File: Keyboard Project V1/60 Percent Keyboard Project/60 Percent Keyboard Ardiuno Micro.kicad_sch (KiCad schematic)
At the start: 126 parts, among them J1 Analog, J2 Digital

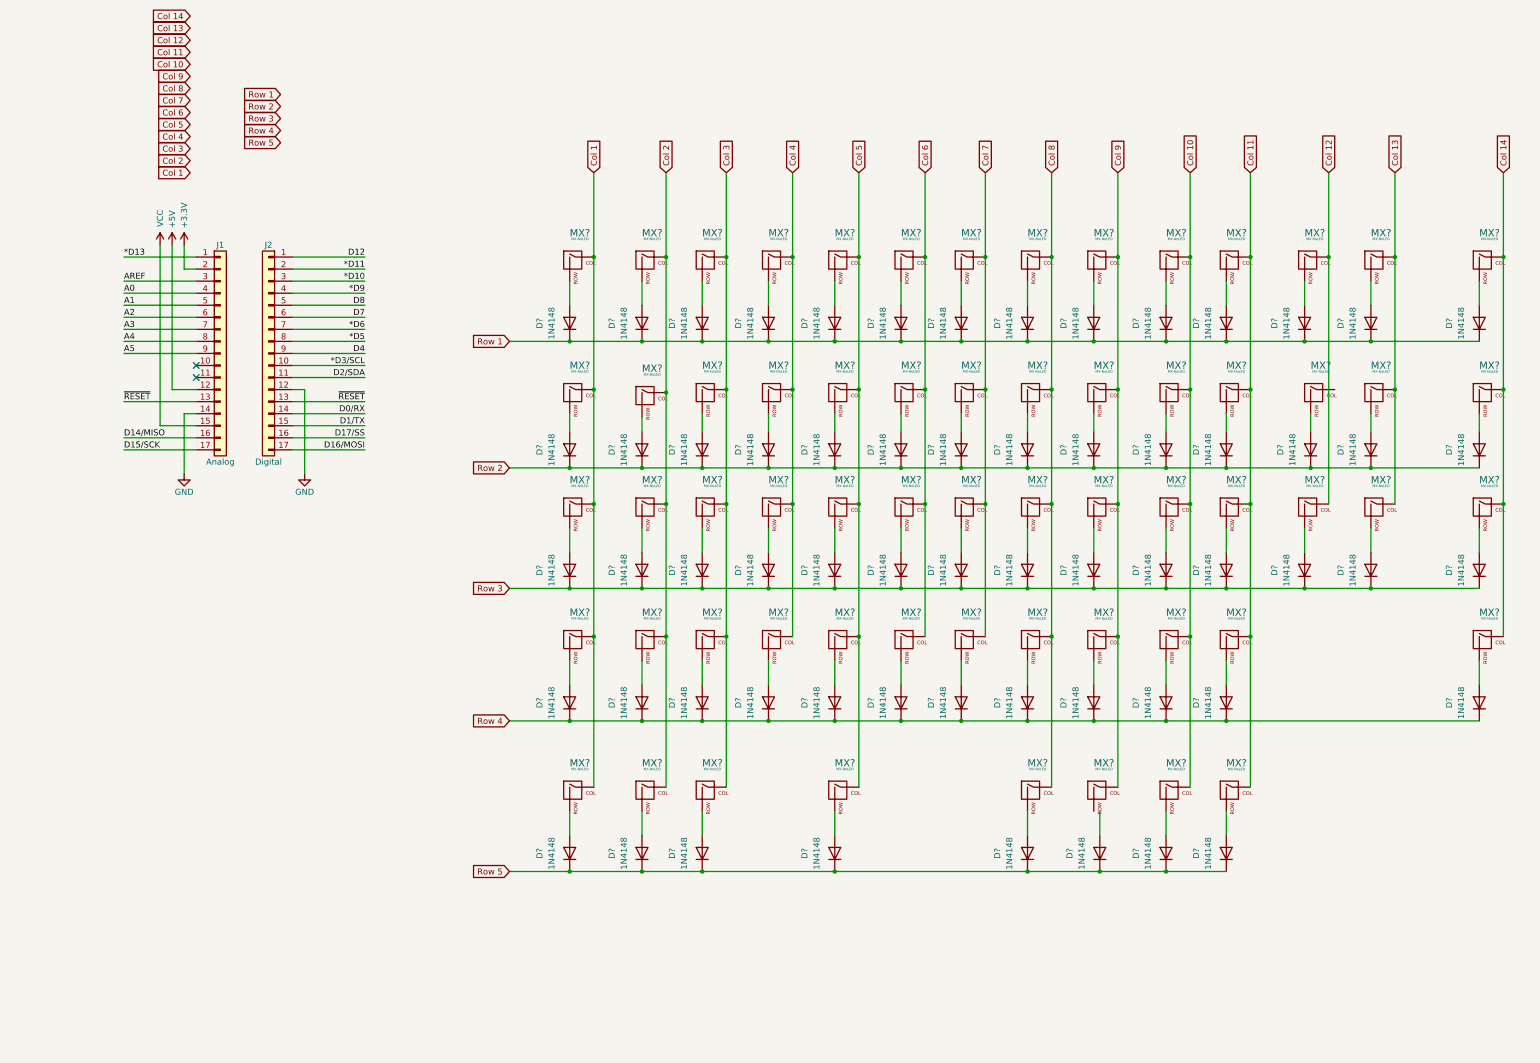
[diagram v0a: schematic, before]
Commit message: updated version of version 1 and currently in the PCB editor. Almost done with version one and may work on version V1.1 after this
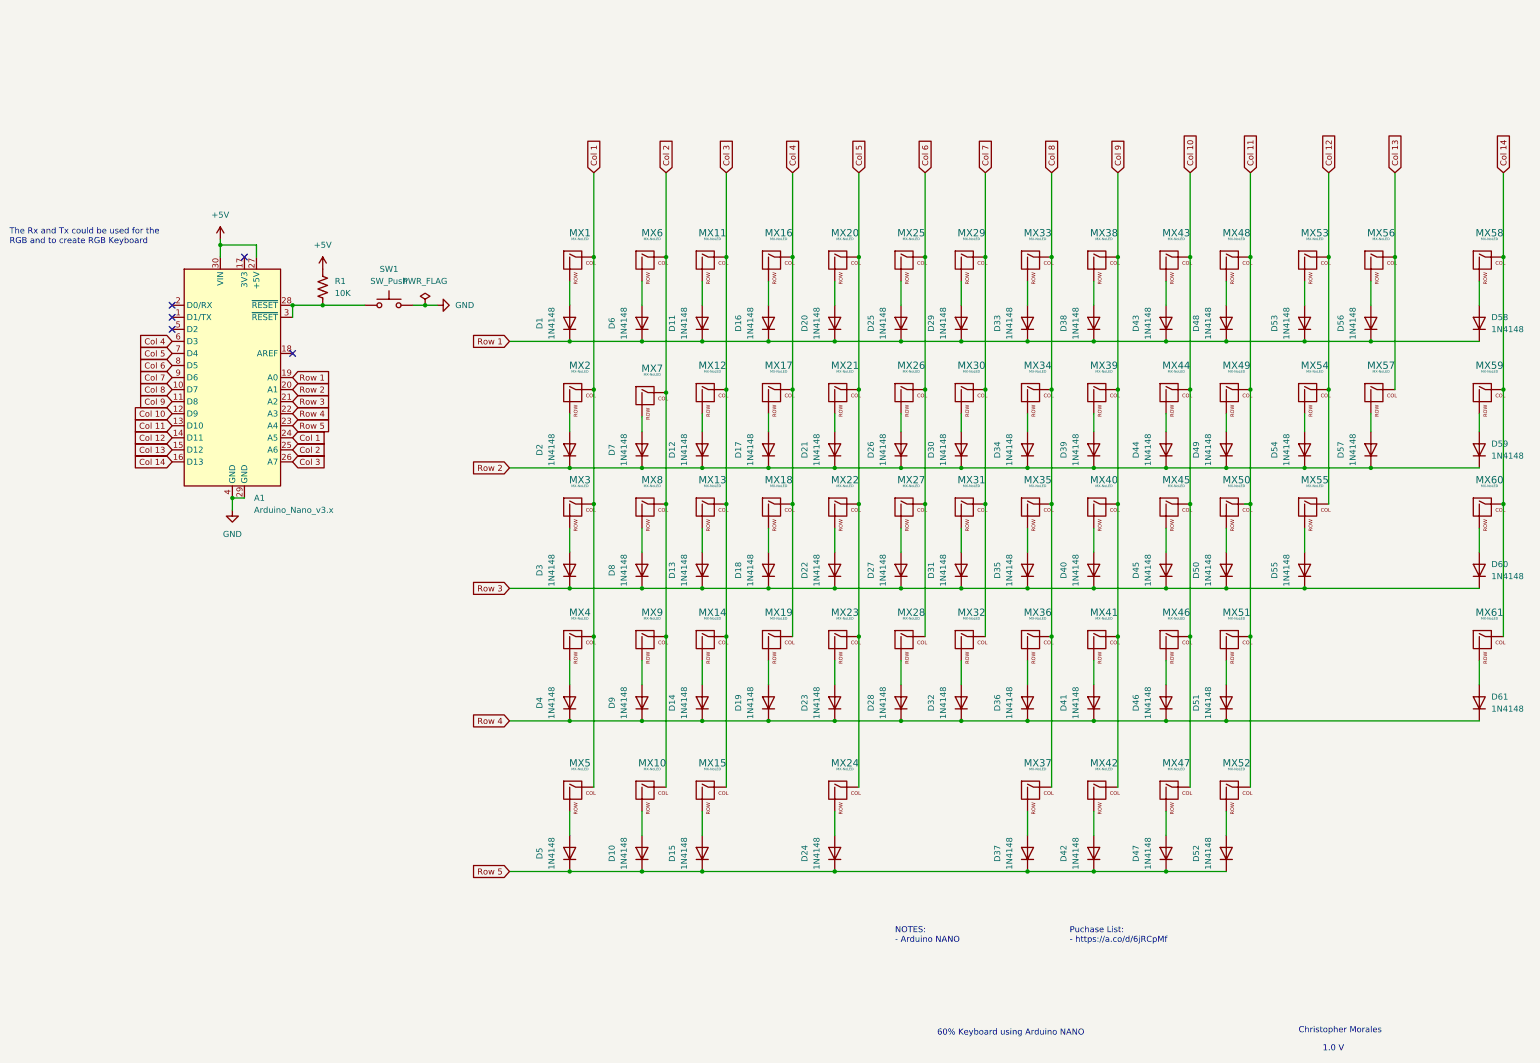
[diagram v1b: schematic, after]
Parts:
- removed D?: 1N4148, Diode_THT:D_DO-35_SOD27_P7.62mm_Horizontal, symbol Diode:1N4148
- removed J1: Analog, Connector_PinHeader_2.54mm:PinHeader_1x17_P2.54mm_Vertical, symbol Connector_Generic:Conn_01x17
- removed J2: Digital, Connector_PinHeader_2.54mm:PinHeader_1x17_P2.54mm_Vertical, symbol Connector_Generic:Conn_01x17
- removed MX?: MX-NoLED, symbol MX_Alps_Hybrid:MX-NoLED
- added A1: Arduino_Nano_v3.x, Module:Arduino_Nano, symbol MCU_Module:Arduino_Nano_v3.x
- added R1: 10K, Resistor_THT:R_Axial_DIN0207_L6.3mm_D2.5mm_P10.16mm_Horizontal, symbol Device:R_US
- added SW1: SW_Push, Button_Switch_THT:SW_PUSH_6mm, symbol Switch:SW_Push
- MX1, MX11, MX12, MX13, MX14, MX16, MX17, MX18, MX19, MX20, MX21, MX22, MX23, MX25, MX26, MX27, MX28, MX29, MX30, MX31, MX32, MX33, MX34, MX35, MX36, MX38, MX39, MX40, MX41, MX43, MX44, MX45, MX46, MX48, MX49, MX50, MX51, MX53, MX54, MX55, MX56, MX57, MX6, MX7, MX8, MX9: renamed from MX?; footprint (none) -> Switch_Keyboard_Cherry_MX:SW_Cherry_MX_PCB_1.00u
- MX10, MX15, MX37, MX42, MX47, MX5, MX52: renamed from MX?; footprint (none) -> Switch_Keyboard_Cherry_MX:SW_Cherry_MX_PCB_1.25u
- MX2, MX59: renamed from MX?; footprint (none) -> Switch_Keyboard_Cherry_MX:SW_Cherry_MX_PCB_1.50u
- MX24: renamed from MX?; footprint (none) -> Switch_Keyboard_Cherry_MX:SW_Cherry_MX_PCB_6.25u
- MX3: renamed from MX?; footprint (none) -> Switch_Keyboard_Cherry_MX:SW_Cherry_MX_PCB_1.75u
- MX4, MX60: renamed from MX?; footprint (none) -> Switch_Keyboard_Cherry_MX:SW_Cherry_MX_PCB_2.25u
- MX58: renamed from MX?; footprint (none) -> Switch_Keyboard_Cherry_MX:SW_Cherry_MX_PCB_2.00u
- MX61: renamed from MX?; footprint (none) -> Switch_Keyboard_Cherry_MX:SW_Cherry_MX_PCB_2.75u
- gave numbers to parts that had none: 61
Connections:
- net +5V: now also A1.27 (+5V), A1.30 (VIN), R1.2
- net Col 1: now also A1.24 (A5)
- net Col 10: now also A1.12 (D9)
- net Col 11: now also A1.13 (D10)
- net Col 12: now also MX55.1 (COL), A1.14 (D11)
- net Col 13: now also A1.15 (D12)
- net Col 14: now also A1.16 (D13)
- net Col 2: now also A1.25 (A6)
- net Col 3: now also A1.26 (A7)
- net Col 4: now also A1.6 (D3)
- net Col 5: now also A1.7 (D4)
- net Col 6: now also A1.8 (D5)
- net Col 7: now also A1.9 (D6)
- net Col 8: now also A1.10 (D7)
- net Col 9: now also A1.11 (D8)
- net GND: now also A1.29 (GND), A1.4 (GND), SW1.2
- net Row 1: now also A1.19 (A0)
- net Row 2: now also D54.1 (K), A1.20 (A1); no longer D55.1 (K)
- net Row 3: now also D55.1 (K), A1.21 (A2); no longer D54.1 (K)
- net Row 4: now also A1.22 (A3)
- net Row 5: now also A1.23 (A4)
- net at MX42.2 (ROW): now also D42.2 (A)
- new net: A1.28 (~{RESET}), A1.3 (~{RESET}), R1.1, SW1.1
- no-connect marks 2 -> 5
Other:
- note added: "1.0 V"
- note added: "60% Keyboard using Arduino NANO"
- note added: "Christopher Morales"
- note added: "NOTES: - Arduino NANO"
- note added: "Puchase List: - https://a.co/d/6jRCpMf"
- note added: "The Rx and Tx could be used for the RGB and to create RGB Keyboard"
- moved on the sheet: D42, D54, D55, MX54, MX55

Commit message: Finally completed 1 versiongit add .!
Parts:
- removed R1: 10K, Resistor_THT:R_Axial_DIN0207_L6.3mm_D2.5mm_P10.16mm_Horizontal, symbol Device:R_US
- removed SW1: SW_Push, Button_Switch_THT:SW_PUSH_6mm, symbol Switch:SW_Push
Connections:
- net at A1.28 (~{RESET}): no longer A1.3 (~{RESET})
- net GND: no longer names the net of A1.29 (GND)
- net GND: no longer A1.4 (GND)
- no-connect marks 5 -> 9
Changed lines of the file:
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@@
   (junction (at 110.49 96.52) (diameter 0) (color 0 0 0 0)
   )
-  (junction (at 39.37 77.47) (diameter 0) (color 0 0 0 0)
-  )
   (junction (at 212.09 106.68) (diameter 0) (color 0 0 0 0)
   )
@@
   (junction (at 138.43 71.12) (diameter 0) (color 0 0 0 0)
   )
-  (junction (at 52.07 36.83) (diameter 0) (color 0 0 0 0)
-  )
   (junction (at 130.81 26.67) (diameter 0) (color 0 0 0 0)
   )
@@
   (junction (at 226.06 106.68) (diameter 0) (color 0 0 0 0)
   )
-  (junction (at 80.01 36.83) (diameter 0) (color 0 0 0 0)
-  )
   (junction (at 130.81 55.245) (diameter 0) (color 0 0 0 0)
   )
@@
   (junction (at 171.45 78.74) (diameter 0) (color 0 0 0 0)
   )
-  (junction (at 58.42 36.83) (diameter 0) (color 0 0 0 0)
-  )
   (junction (at 241.3 54.61) (diameter 0) (color 0 0 0 0)
   )
@@
   )
   (no_connect (at 52.07 46.99))
+  (no_connect (at 52.07 36.83))
+  (no_connect (at 52.07 39.37))
   (no_connect (at 26.67 36.83))
+  (no_connect (at 39.37 77.47))
+  (no_connect (at 41.91 77.47))
   (no_connect (at 26.67 41.91))
   (no_connect (at 26.67 39.37))
@@
     (stroke (width 0) (type default) (color 0 0 0 0))
   )
-  (wire (pts (xy 58.42 36.83) (xy 67.31 36.83))
-    (stroke (width 0) (type default) (color 0 0 0 0))
-  )
   (wire (pts (xy 207.01 83.82) (xy 207.01 88.9))
     (stroke (width 0) (type default) (color 0 0 0 0))
@@
     (stroke (width 0) (type default) (color 0 0 0 0))
   )
-  (wire (pts (xy 80.01 36.83) (xy 82.55 36.83))
-    (stroke (width 0) (type default) (color 0 0 0 0))
-  )
   (wire (pts (xy 166.37 156.21) (xy 207.01 156.21))
     (stroke (width 0) (type default) (color 0 0 0 0))
@@
     (stroke (width 0) (type default) (color 0 0 0 0))
   )
-  (wire (pts (xy 52.07 36.83) (xy 52.07 39.37))
-    (stroke (width 0) (type default) (color 0 0 0 0))
-  )
   (wire (pts (xy 152.4 31.75) (xy 152.4 36.83))
     (stroke (width 0) (type default) (color 0 0 0 0))
@@
     (stroke (width 0) (type default) (color 0 0 0 0))
   )
-  (wire (pts (xy 77.47 36.83) (xy 80.01 36.83))
-    (stroke (width 0) (type default) (color 0 0 0 0))
-  )
   (wire (pts (xy 125.73 143.51) (xy 125.73 148.59))
     (stroke (width 0) (type default) (color 0 0 0 0))
@@
     (stroke (width 0) (type default) (color 0 0 0 0))
   )
-  (wire (pts (xy 39.37 77.47) (xy 39.37 80.01))
-    (stroke (width 0) (type default) (color 0 0 0 0))
-  )
   (wire (pts (xy 302.26 83.82) (xy 302.26 88.9))
     (stroke (width 0) (type default) (color 0 0 0 0))
@@
     (stroke (width 0) (type default) (color 0 0 0 0))
   )
-  (wire (pts (xy 41.91 77.47) (xy 39.37 77.47))
-    (stroke (width 0) (type default) (color 0 0 0 0))
-  )
   (wire (pts (xy 152.4 71.12) (xy 166.37 71.12))
     (stroke (width 0) (type default) (color 0 0 0 0))
@@
     (stroke (width 0) (type default) (color 0 0 0 0))
   )
-  (wire (pts (xy 52.07 36.83) (xy 58.42 36.83))
-    (stroke (width 0) (type default) (color 0 0 0 0))
-  )
   (wire (pts (xy 166.37 83.82) (xy 166.37 88.9))
     (stroke (width 0) (type default) (color 0 0 0 0))
@@
     (pin "2")
   )
-  (symbol (lib_id "power:PWR_FLAG") (at 80.01 36.83 0) (unit 1)
-    (in_bom yes) (on_board yes) (fields_autoplaced)
-    (property "Reference" "#FLG0102" (id 0) (at 80.01 34.925 0)
-      (effects (font (size 1.27 1.27)) hide)
-    )
-    (property "Value" "PWR_FLAG" (id 1) (at 80.01 31.75 0))
-    (property "Footprint" "" (id 2) (at 80.01 36.83 0)
-      (effects (font (size 1.27 1.27)) hide)
-    )
-    (property "Datasheet" "~" (id 3) (at 80.01 36.83 0)
-      (effects (font (size 1.27 1.27)) hide)
-    )
-    (pin "1")
-  )
   (symbol (lib_id "Diode:1N4148") (at 220.98 92.71 90) (unit 1)
     (in_bom yes) (on_board yes)
@@
     (pin "2")
   )
-  (symbol (lib_id "power:+5V") (at 58.42 29.21 0) (unit 1)
-    (in_bom yes) (on_board yes) (fields_autoplaced)
-    (property "Reference" "#PWR03" (id 0) (at 58.42 33.02 0)
-      (effects (font (size 1.27 1.27)) hide)
-    )
-    (property "Value" "+5V" (id 1) (at 58.42 24.13 0))
-    (property "Footprint" "" (id 2) (at 58.42 29.21 0)
-      (effects (font (size 1.27 1.27)) hide)
-    )
-    (property "Datasheet" "" (id 3) (at 58.42 29.21 0)
-      (effects (font (size 1.27 1.27)) hide)
-    )
-    (pin "1")
-  )
   (symbol (lib_id "Diode:1N4148") (at 125.73 40.64 90) (unit 1)
     (in_bom yes) (on_board yes) (fields_autoplaced)
@@
     (pin "2")
   )
-  (symbol (lib_id "power:GND") (at 39.37 80.01 0) (unit 1)
-    (in_bom yes) (on_board yes) (fields_autoplaced)
-    (property "Reference" "#PWR0102" (id 0) (at 39.37 86.36 0)
-      (effects (font (size 1.27 1.27)) hide)
-    )
-    (property "Value" "GND" (id 1) (at 39.37 85.09 0))
-    (property "Footprint" "" (id 2) (at 39.37 80.01 0)
-      (effects (font (size 1.27 1.27)) hide)
-    )
-    (property "Datasheet" "" (id 3) (at 39.37 80.01 0)
-      (effects (font (size 1.27 1.27)) hide)
-    )
-    (pin "1")
-  )
   (symbol (lib_id "Diode:1N4148") (at 138.43 40.64 90) (unit 1)
     (in_bom yes) (on_board yes) (fields_autoplaced)
@@
     (pin "2")
   )
-  (symbol (lib_id "Switch:SW_Push") (at 72.39 36.83 0) (unit 1)
-    (in_bom yes) (on_board yes) (fields_autoplaced)
-    (property "Reference" "SW1" (id 0) (at 72.39 29.21 0))
-    (property "Value" "SW_Push" (id 1) (at 72.39 31.75 0))
-    (property "Footprint" "Button_Switch_THT:SW_PUSH_6mm" (id 2) (at 72.39 31.75 0)
-      (effects (font (size 1.27 1.27)) hide)
-    )
-    (property "Datasheet" "~" (id 3) (at 72.39 31.75 0)
-      (effects (font (size 1.27 1.27)) hide)
-    )
-    (pin "1")
-    (pin "2")
-  )
   (symbol (lib_id "Diode:1N4148") (at 193.04 40.64 90) (unit 1)
     (in_bom yes) (on_board yes) (fields_autoplaced)
@@
     (pin "2")
   )
-  (symbol (lib_id "Device:R_US") (at 58.42 33.02 180) (unit 1)
-    (in_bom yes) (on_board yes) (fields_autoplaced)
-    (property "Reference" "R1" (id 0) (at 60.96 31.7499 0)
-      (effects (font (size 1.27 1.27)) (justify right))
-    )
-    (property "Value" "10K" (id 1) (at 60.96 34.2899 0)
-      (effects (font (size 1.27 1.27)) (justify right))
-    )
-    (property "Footprint" "Resistor_THT:R_Axial_DIN0207_L6.3mm_D2.5mm_P10.16mm_Horizontal" (id 2) (at 57.404 32.766 90)
-      (effects (font (size 1.27 1.27)) hide)
-    )
-    (property "Datasheet" "~" (id 3) (at 58.42 33.02 0)
-      (effects (font (size 1.27 1.27)) hide)
-    )
-    (pin "1")
-    (pin "2")
-  )
-  (symbol (lib_id "power:GND") (at 82.55 36.83 90) (unit 1)
-    (in_bom yes) (on_board yes) (fields_autoplaced)
-    (property "Reference" "#PWR0103" (id 0) (at 88.9 36.83 0)
-      (effects (font (size 1.27 1.27)) hide)
-    )
-    (property "Value" "GND" (id 1) (at 86.36 36.8299 90)
-      (effects (font (size 1.27 1.27)) (justify right))
-    )
-    (property "Footprint" "" (id 2) (at 82.55 36.83 0)
-      (effects (font (size 1.27 1.27)) hide)
-    )
-    (property "Datasheet" "" (id 3) (at 82.55 36.83 0)
-      (effects (font (size 1.27 1.27)) hide)
-    )
-    (pin "1")
-  )
   (symbol (lib_id "Diode:1N4148") (at 265.43 92.71 90) (unit 1)
     (in_bom yes) (on_board yes) (fields_autoplaced)
@@
   )
   (symbol_instances
-    (path "/174c0248-d621-45af-8863-9a63f89f8b5c"
-      (reference "#FLG0102") (unit 1) (value "PWR_FLAG") (footprint "")
-    )
-    (path "/35993f94-da82-4ecc-8b52-82499756777c"
-      (reference "#PWR03") (unit 1) (value "+5V") (footprint "")
-    )
     (path "/68246a70-a95c-40be-8630-41a0015fd436"
       (reference "#PWR0101") (unit 1) (value "+5V") (footprint "")
     )
-    (path "/3f6978cb-0477-465c-b975-a21e1db3159b"
-      (reference "#PWR0102") (unit 1) (value "GND") (footprint "")
-    )
-    (path "/c693be29-80ff-4a09-83f7-165b5c02f3b7"
-      (reference "#PWR0103") (unit 1) (value "GND") (footprint "")
-    )
     (path "/bc2bc923-62d1-49a6-be91-d355066f86c4"
       (reference "A1") (unit 1) (value "Arduino_Nano_v3.x") (footprint "Module:Arduino_Nano")
@@
       (reference "MX61") (unit 1) (value "MX-NoLED") (footprint "Switch_Keyboard_Cherry_MX:SW_Cherry_MX_PCB_2.75u")
     )
-    (path "/c1f60d30-97f4-4d20-bcaf-009a3d15cc2e"
-      (reference "R1") (unit 1) (value "10K") (footprint "Resistor_THT:R_Axial_DIN0207_L6.3mm_D2.5mm_P10.16mm_Horizontal")
-    )
-    (path "/b4d6b699-0aae-4c07-8725-f56a07c224c0"
-      (reference "SW1") (unit 1) (value "SW_Push") (footprint "Button_Switch_THT:SW_PUSH_6mm")
-    )
   )
